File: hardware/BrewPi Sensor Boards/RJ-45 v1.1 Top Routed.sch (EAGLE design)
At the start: 6 parts, among them J1 RJ45-8X

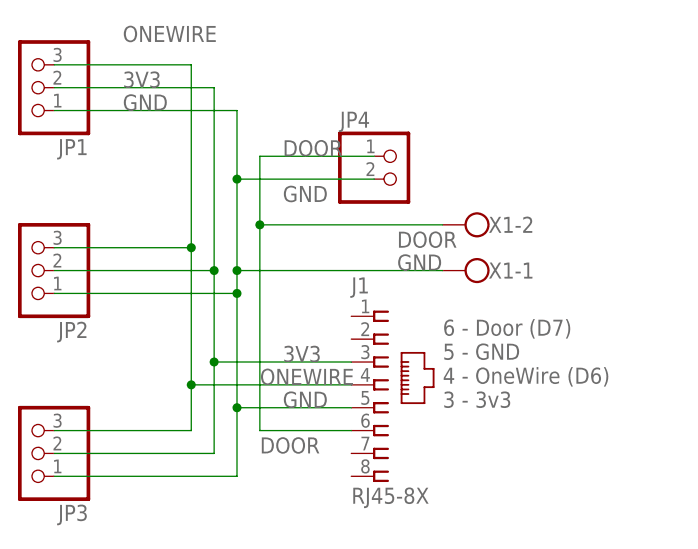
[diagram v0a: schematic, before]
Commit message: Updating docs & adding new eagle schematics
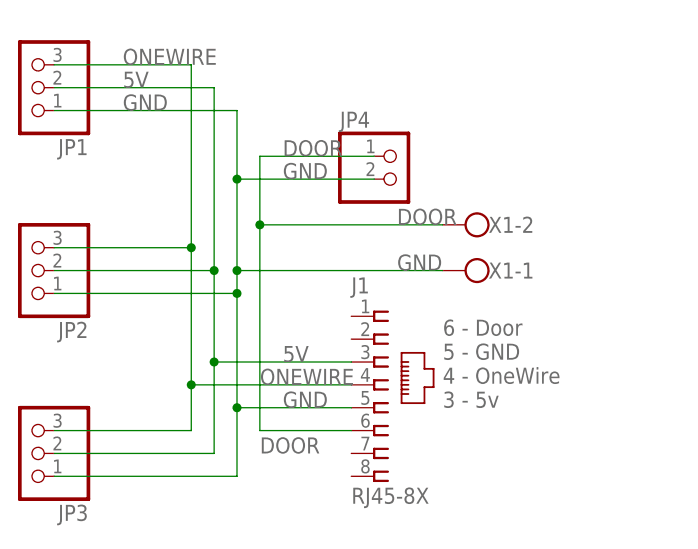
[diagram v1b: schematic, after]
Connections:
- net 3V3 renamed 5V
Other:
- note added: "6 - Door 5 - GND 4 - OneWire 3 - 5v"
- note removed: "6 - Door (D7) 5 - GND 4 - OneWire (D6) 3 - 3v3"
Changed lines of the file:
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@@
 <?xml version="1.0" encoding="utf-8"?>
 <!DOCTYPE eagle SYSTEM "eagle.dtd">
-<eagle version="7.3.0">
+<eagle version="9.5.2">
 <drawing>
 <settings>
 <setting alwaysvectorfont="no"/>
+<setting keepoldvectorfont="yes"/>
 <setting verticaltext="up"/>
 </settings>
@@
 <sheet>
 <plain>
-<text x="71.12" y="38.1" size="1.778" layer="95">6 - Door (D7)
+<text x="71.12" y="38.1" size="1.778" layer="95">6 - Door
 5 - GND
-4 - OneWire (D6)
-3 - 3v3</text>
+4 - OneWire
+3 - 5v</text>
 </plain>
 <instances>
-<instance part="J1" gate="G$1" x="63.5" y="40.64"/>
-<instance part="JP1" gate="A" x="25.4" y="73.66" rot="R180"/>
-<instance part="JP2" gate="A" x="25.4" y="53.34" rot="R180"/>
-<instance part="JP3" gate="A" x="25.4" y="33.02" rot="R180"/>
-<instance part="JP4" gate="G$1" x="66.04" y="63.5"/>
-<instance part="X1" gate="-1" x="76.2" y="53.34" rot="R180"/>
-<instance part="X1" gate="-2" x="76.2" y="58.42" rot="R180"/>
+<instance part="J1" gate="G$1" x="63.5" y="40.64" smashed="yes">
+<attribute name="NAME" x="60.96" y="50.8" size="1.778" layer="95"/>
+<attribute name="VALUE" x="60.96" y="27.432" size="1.778" layer="96"/>
+</instance>
+<instance part="JP1" gate="A" x="25.4" y="73.66" smashed="yes" rot="R180">
+<attribute name="NAME" x="31.75" y="67.945" size="1.778" layer="95" rot="R180"/>
+<attribute name="VALUE" x="31.75" y="81.28" size="1.778" layer="96" rot="R180"/>
+</instance>
+<instance part="JP2" gate="A" x="25.4" y="53.34" smashed="yes" rot="R180">
+<attribute name="NAME" x="31.75" y="47.625" size="1.778" layer="95" rot="R180"/>
+<attribute name="VALUE" x="31.75" y="60.96" size="1.778" layer="96" rot="R180"/>
+</instance>
+<instance part="JP3" gate="A" x="25.4" y="33.02" smashed="yes" rot="R180">
+<attribute name="NAME" x="31.75" y="27.305" size="1.778" layer="95" rot="R180"/>
+<attribute name="VALUE" x="31.75" y="40.64" size="1.778" layer="96" rot="R180"/>
+</instance>
+<instance part="JP4" gate="G$1" x="66.04" y="63.5" smashed="yes">
+<attribute name="NAME" x="59.69" y="69.215" size="1.778" layer="95"/>
+<attribute name="VALUE" x="59.69" y="58.42" size="1.778" layer="96"/>
+</instance>
+<instance part="X1" gate="-1" x="76.2" y="53.34" smashed="yes" rot="R180">
+<attribute name="NAME" x="76.2" y="52.451" size="1.778" layer="95"/>
+</instance>
+<instance part="X1" gate="-2" x="76.2" y="58.42" smashed="yes" rot="R180">
+<attribute name="VALUE" x="78.74" y="62.103" size="1.778" layer="96" rot="R180"/>
+<attribute name="NAME" x="76.2" y="57.531" size="1.778" layer="95"/>
+</instance>
 </instances>
 <busses>
@@
 <wire x1="43.18" y1="76.2" x2="43.18" y2="55.88" width="0.1524" layer="91"/>
 <wire x1="43.18" y1="55.88" x2="43.18" y2="40.64" width="0.1524" layer="91"/>
-<label x="35.56" y="78.74" size="1.778" layer="95"/>
+<label x="35.56" y="76.2" size="1.778" layer="95"/>
 <pinref part="JP2" gate="A" pin="3"/>
 <wire x1="43.18" y1="40.64" x2="43.18" y2="35.56" width="0.1524" layer="91"/>
@@
 </segment>
 </net>
-<net name="3V3" class="0">
+<net name="5V" class="0">
 <segment>
 <wire x1="45.72" y1="53.34" x2="45.72" y2="73.66" width="0.1524" layer="91"/>
@@
 <wire x1="48.26" y1="63.5" x2="48.26" y2="71.12" width="0.1524" layer="91"/>
 <label x="35.56" y="71.12" size="1.778" layer="95"/>
-<label x="53.34" y="60.96" size="1.778" layer="95"/>
+<label x="53.34" y="63.5" size="1.778" layer="95"/>
 <pinref part="JP2" gate="A" pin="1"/>
 <wire x1="27.94" y1="50.8" x2="48.26" y2="50.8" width="0.1524" layer="91"/>
@@
 <wire x1="71.12" y1="58.42" x2="50.8" y2="58.42" width="0.1524" layer="91"/>
 <junction x="50.8" y="58.42"/>
-<label x="66.04" y="55.88" size="1.778" layer="95"/>
+<label x="66.04" y="58.42" size="1.778" layer="95"/>
 </segment>
 </net>
